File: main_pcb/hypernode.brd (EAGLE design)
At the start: 92.5 x 100 mm, 134 parts, among them IC1 74HCT245D, J1 AVR_SPI_PRG_62X3_LOCK, U1 MAX488, U2 PCA9685, U3 VOLTAGE_REGULATORDPACK, U4 ATMEGA328P, U5 MAX3421E, X1 USB-A-H, X10 JST-XH-03-PIN-LONG-PAD, X2 JST-XH-CONNECTOR-02-PIN, X4 JST-XH-CONNECTOR-02-PIN, X7 JST-XH-03-PIN-LONG-PAD, X8 JST-XH-03-PIN-LONG-PAD, X9 JST-XH-03-PIN-LONG-PAD, Y1 8MHZ

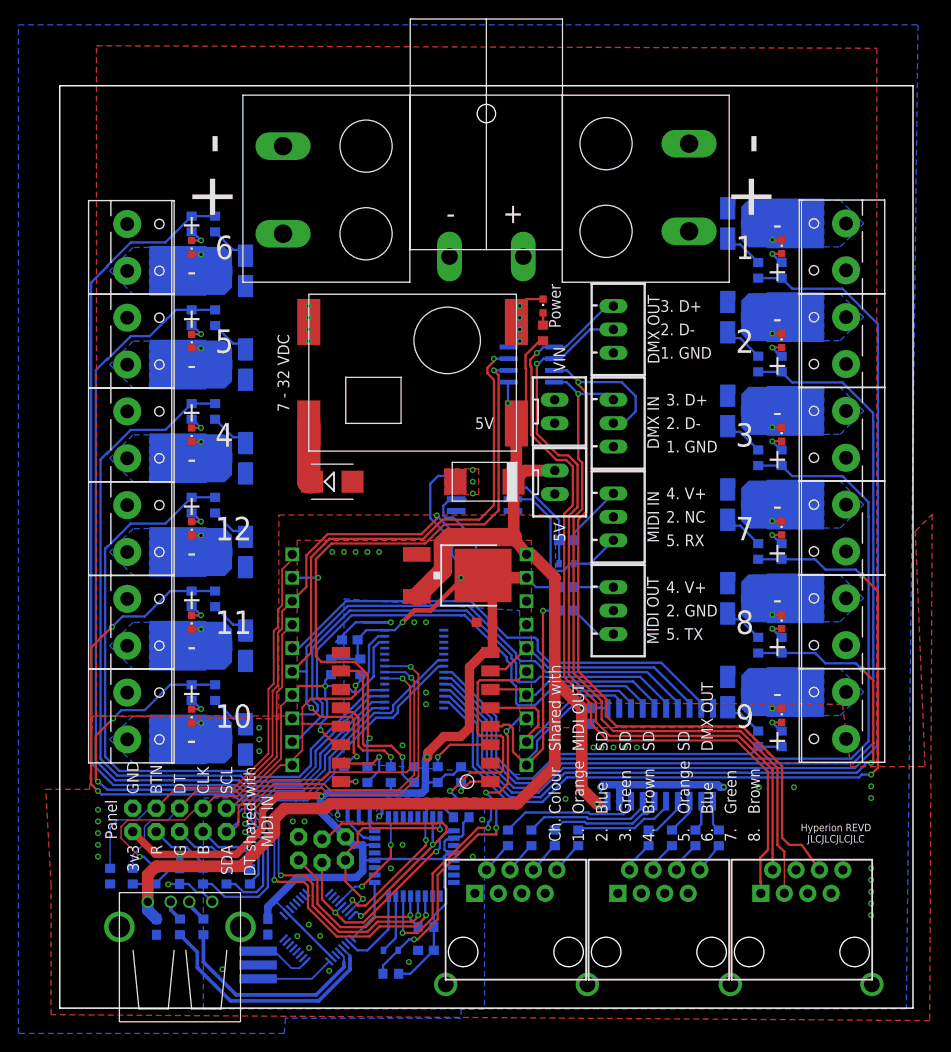
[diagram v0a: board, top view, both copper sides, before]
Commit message: remove unnecessary components from main pcb
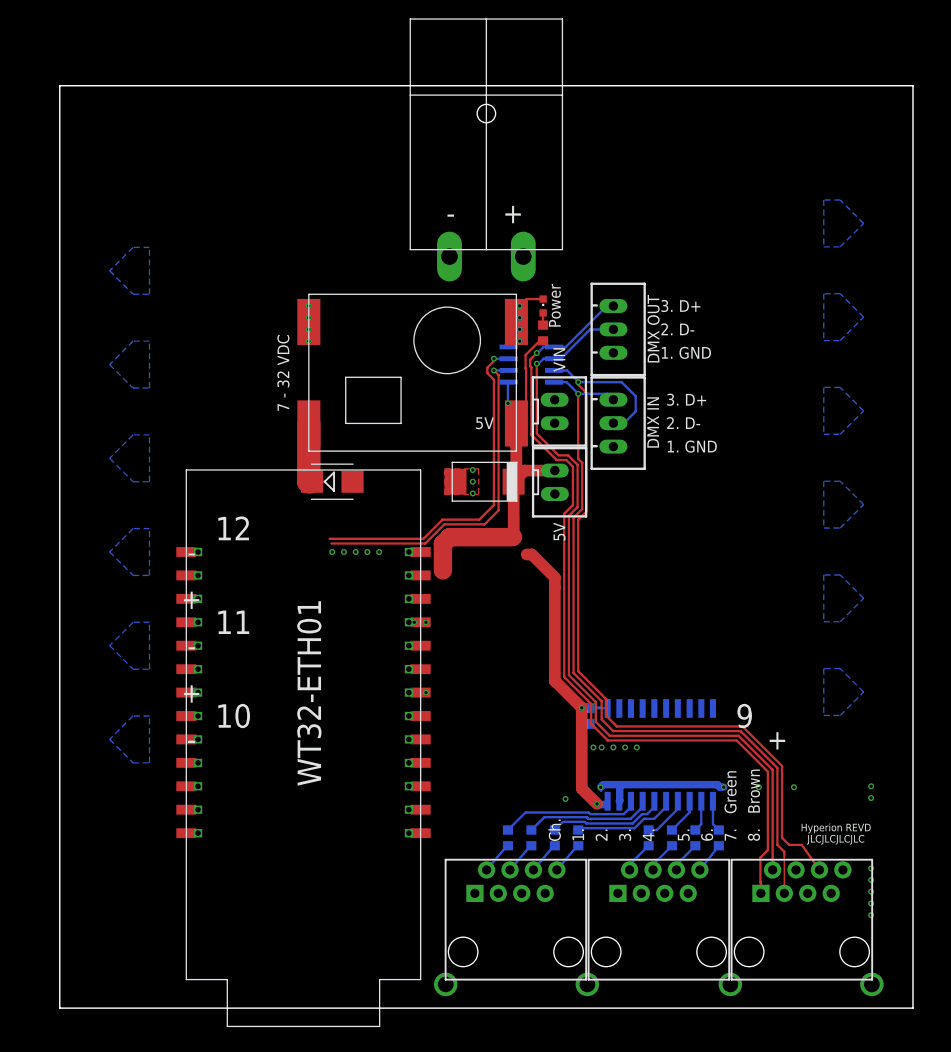
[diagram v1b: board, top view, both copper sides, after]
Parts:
- removed C2, C3, C4, C6, C7: 100nF, Multischriever:ADAFRUIT_C0603
- removed C8: 1uF, Multischriever:ADAFRUIT_C0603
- removed C9: 4.7uF, Multischriever:ADAFRUIT_C0603
- removed D1, D3: (no value), Multischriever:ADAFRUIT_SOD-523
- removed HCPL0453: HCPL0700, optocoupler:SOIC08
- removed J1: AVR_SPI_PRG_62X3_LOCK, SparkFun-Connectors:2X3_LOCK
- removed LED11, LED13, LED14, LED15, LED16, LED17, LED18, LED2, LED3, LED5, LED7, LED9: (no value), Multischriever:ADAFRUIT_CHIPLED_0603
- removed R12, R15, R18, R19, R22, R23, R26, R27, R3, R30, R31, R32, R33, R34, R35, R36, R37, R38, R39, R40, R41, R5: (no value), Multischriever:ADAFRUIT_R0603
- removed R13, R45, R46, R47: 180R, Multischriever:ADAFRUIT_R0603
- removed R14: 1K, Multischriever:ADAFRUIT_R0603
- removed R21, R24: 1k, Multischriever:ADAFRUIT_R0603
- removed R25, R28, R29, R42: 10k, Multischriever:ADAFRUIT_R0603
- removed R43, R44, R57: 4k7, Multischriever:ADAFRUIT_R0603
- removed R48, R50, R55, R56: 10K, Multischriever:ADAFRUIT_R0603
- removed R49, R9: 470R, Multischriever:ADAFRUIT_R0603
- removed R52: 100R, Multischriever:ADAFRUIT_R0603
- removed R53, R54, R6, R7: 33R, Multischriever:ADAFRUIT_R0603
- removed R8: 220R, Multischriever:ADAFRUIT_R0603
- removed REMOTE: M05X2NO_SILK, SparkFun-Connectors:2X5_NOSILK
- removed U$1: ESP32POE, Multischriever:ESP32POE
- removed U$10, U$12, U$14, U$16, U$18, U$19, U$20, U$21, U$22, U$23, U$5, U$7: NCV8401_LOAD_SWITCH'DPAK+SOT23', Multischriever:DPACK+SOT23
- removed U$2, U$6: BIGTERMINAL, Multischriever:BIGTERMINAL2P
- removed U$24: 12MHz, adafruit:AWCSR
- removed U$9: ESP8266_ESP12NOSILK, Multischriever:ESP8266-ESP12_ESP8266-ESP12_NOSILK
- removed U2: PCA9685, SparkFun-DigitalIC:TSSOP-28_4MM
- removed U3: VOLTAGE_REGULATORDPACK, Multischriever:SPARKFUN-POWERIC_V-REG_DPACK
- removed U4: ATMEGA328P, SparkFun-DigitalIC:TQFP32-08
- removed U5: MAX3421E, SparkFun-DigitalIC:TQFP32-5MM
- removed X1: USB-A-H, con-usb:USB-A-H
- removed X10, X9: JST-XH-03-PIN-LONG-PAD, Rembrandt Electronics - JST XH Connectors v1-0:JST-XH-03-PACKAGE-LONG-PAD
- removed X11, X14, X16, X17, X19, X21, X22, X23, X24, X25, X26, X3: (no value), Multischriever:CON-WAGO-508_W237-132PLUGGABLE
- removed Y1: 8MHZ, SparkFun-FreqCtrl:RESONATOR-SMD
- added U$17: WT32-ETH01, Multischriever:WT32-ETH01
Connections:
- removed net ENCA: R48.2, REMOTE.8, U$1.GPI34_BUT1
- removed net ENCBTN: R49.2, REMOTE.4, U$1.GPI39
- removed net MIDIIN: R50.2, R52.2, REMOTE.6, U$1.GPI35
- removed net N$1: R45.1, REMOTE.3
- removed net N$11: R45.2, U2.20
- removed net N$12: R46.1, REMOTE.5
- removed net N$14: R6.1, X10.1
- removed net N$15: R7.1, X10.3
- removed net N$17: D1.A, HCPL0453.3, X9.3
- removed net N$19: R5.1, U$7.B, U$7.B_
- removed net N$20: R8.1, X9.1
- removed net N$21: D1.K, HCPL0453.2, R8.2
- removed net N$22: LED2.A, R3.1
- removed net N$23: R29.1, U$9.9
- removed net N$24: LED2.C, U$7.C, U$7.C_, X3.2
- removed net N$27: R42.1, U$9.11
- removed net N$29: R21.2, U$9.8
- removed net N$30: R24.2, U$9.7
- removed net N$31: R28.2, U$9.4
- removed net N$32: R25.2, U$9.2
- removed net N$33: R47.1, REMOTE.7
- removed net N$35: R15.1, U$10.B, U$10.B_
- removed net N$36: LED5.A, R12.1
- removed net N$37: LED5.C, U$10.C, U$10.C_, X11.2
- removed net N$39: HCPL0453.6, R52.1, R9.2
- removed net N$40: U4.7, Y1.1
- removed net N$41: U4.8, Y1.3
- removed net N$42: U4.9, U5.12
- removed net N$43: R54.1, X1.D+
- removed net N$44: R53.1, X1.D-
- removed net N$45: LED3.C, U$5.C, U$5.C_, X17.2
- removed net N$46: R14.1, U$5.B, U$5.B_
- removed net N$47: R19.1, U$12.B, U$12.B_
- removed net N$48: LED7.A, R18.1
- removed net N$49: LED7.C, U$12.C, U$12.C_, X14.2
- removed net N$50: R53.2, U5.20
- removed net N$51: R54.2, U5.21
- removed net N$52: U$24.3, U5.24
- removed net N$53: U$24.1, U5.25
- removed net N$54: U4.32, U5.18
- removed net N$55: U4.1, U5.17
- removed net N$56: J1.4, U4.15, U5.16
- removed net N$57: J1.1, U4.16, U5.15
- removed net N$58: J1.3, U4.17, U5.13
- removed net N$59: R23.1, U$14.B, U$14.B_
- removed net N$60: LED9.A, R22.1
- removed net N$61: LED9.C, U$14.C, U$14.C_, X16.2
- removed net N$62: LED3.A, R13.1
- removed net N$63: R56.1, U4.14, U5.14
- removed net N$64: J1.5, R55.1, U4.29
- removed net N$68: D3.K, U4.31
- removed net N$7: R47.2, U2.22
- removed net N$71: R27.1, U$16.B, U$16.B_
- removed net N$72: LED11.A, R26.1
- removed net N$73: LED11.C, U$16.C, U$16.C_, X19.2
- removed net N$77: R31.1, U$18.B, U$18.B_
- removed net N$78: LED13.A, R30.1
- removed net N$79: LED13.C, U$18.C, U$18.C_, X21.2
- removed net N$80: R33.1, U$19.B, U$19.B_
- removed net N$81: LED14.A, R32.1
- removed net N$82: LED14.C, U$19.C, U$19.C_, X22.2
- removed net N$83: R35.1, U$20.B, U$20.B_
- removed net N$84: LED15.A, R34.1
- removed net N$85: LED15.C, U$20.C, U$20.C_, X23.2
- removed net N$86: R37.1, U$21.B, U$21.B_
- removed net N$87: LED16.A, R36.1
- removed net N$88: LED16.C, U$21.C, U$21.C_, X24.2
- removed net N$89: R39.1, U$22.B, U$22.B_
- removed net N$9: R46.2, U2.21
- removed net N$90: LED17.A, R38.1
- removed net N$91: LED17.C, U$22.C, U$22.C_, X25.2
- removed net N$92: R41.1, U$23.B, U$23.B_
- removed net N$93: LED18.A, R40.1
- removed net N$94: LED18.C, U$23.C, U$23.C_, X26.2
- removed net SCL: R44.1, REMOTE.10, U$1.GPIO16_I2C_SCL, U$9.6, U2.26, U4.28
- removed net SDA: R43.1, REMOTE.9, U$1.GPIO13_I2C_SDA, U$9.5, U2.27, U4.27
- removed net T1DRIVE1: R13.2, R14.2, U2.15
- removed net T1DRIVE10: R34.2, R35.2, U2.13
- removed net T1DRIVE11: R32.2, R33.2, U2.12
- removed net T1DRIVE12: R30.2, R31.2, U2.8
- removed net T1DRIVE2: R3.2, R5.2, U2.16
- removed net T1DRIVE3: R12.2, R15.2, U2.17
- removed net T1DRIVE4: R18.2, R19.2, U2.18
- removed net T1DRIVE5: R22.2, R23.2, U2.7
- removed net T1DRIVE6: R26.2, R27.2, U2.6
- removed net T1DRIVE7: R40.2, R41.2, U2.11
- removed net T1DRIVE8: R38.2, R39.2, U2.10
- removed net T1DRIVE9: R36.2, R37.2, U2.9
- removed net USBRX: D3.A, R57.2, U$1.GPIO3_U0RXD
- removed net USBTX: U$1.GPIO1_U0TXD, U4.30
- new net DMXOUT: U$17.P$8, U$17.P_TXD, U1.3
- net +3V3: now also U$17.3V3, U$17.3V3@1, U$17.P_3V3, U$17.P_3V3@1; no longer C2.1, C3.1, C4.1, C6.1, C7.1, C8.1, HCPL0453.8, J1.2, R28.1, R29.2, R42.2, R43.2, R44.2, R48.1, R50.1, R55.2, R56.2, R57.1, R6.2, R9.1, REMOTE.1, U$1.+3V3, U$9.16, U2.28, U3.4, U4.18, U4.20, U4.4, U4.6, U5.2, U5.23
- net +5V: now also U$17.5V, U$17.P_5V; no longer C9.1, U$1.+5V, U3.3, X1.VBUS
- net DMXIN: now also U$17.IO36, U$17.P_IO36; no longer R24.1, U$1.GPI36_U1RXD
- net GND: now also U$17.GND, U$17.GND@1, U$17.GND@2, U$17.GND@3, U$17.GND@4, U$17.P_GND, U$17.P_GND@1, U$17.P_GND@2, U$17.P_GND@3, U$17.P_GND@4; no longer C2.2, C3.2, C4.2, C6.2, C7.2, C8.2, C9.2, HCPL0453.5, J1.6, R25.1, R49.1, REMOTE.2, U$1.GND, U$10.E, U$10.E_, U$12.E, U$12.E_, U$14.E, U$14.E_, U$16.E, U$16.E_, U$18.E, U$18.E_, U$19.E, U$19.E_, U$2.P$1, U$20.E, U$20.E_, U$21.E, U$21.E_, U$22.E, U$22.E_, U$23.E, U$23.E_, U$24.2, U$5.E, U$5.E_, U$6.P$2, U$7.E, U$7.E_, U$9.1, U2.1, U2.14, U2.2, U2.23, U2.24, U2.25, U2.3, U2.4, U2.5, U3.1, U4.21, U4.3, U4.5, U5.19, U5.3, X1.GND, X10.2, Y1.2
- net VDD: no longer U$2.P$2, U$6.P$1, X11.1, X14.1, X16.1, X17.1, X19.1, X21.1, X22.1, X23.1, X24.1, X25.1, X26.1, X3.1
- net WS1: now also U$17.P_RXD, U$17.RXD; no longer R7.2, U$1.GPIO5_SPL_CS, U$9.12
- net WS2: now also U$17.IO4, U$17.P_IO4; no longer U$1.GPIO4_U1TXD, U$9.13
- net WS3: now also U$17.IO14, U$17.P_IO14; no longer U$1.GPIO14_HS2_CLK
- net WS4: now also U$17.IO2, U$17.P_IO2; no longer U$1.GPIO2_HS2_DATA0, U$9.14
- net WS5: now also U$17.IO15, U$17.P_IO15; no longer U$1.GPIO15_HS2_CMD
- net WS6: now also U$17.CFG, U$17.P_CFG; no longer R21.1, U$1.GPIO32, U1.3
- net WS7: now also U$17.IO0, U$17.P_IO0; no longer U$1.GPIO0, U$9.15
- net WS8: now also U$17.485_EN, U$17.P_485_EN; no longer U$1.GPIO33
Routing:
- net +3V3: track 207.2 -> 0.00 mm, vias 5 -> 0
- net WS6: track 120.3 -> 0.00 mm, vias 3 -> 0
- net T1DRIVE7: track 117.1 -> 0.00 mm
- net T1DRIVE1: track 106.3 -> 0.00 mm
- net T1DRIVE8: track 105.9 -> 0.00 mm
- net T1DRIVE2: track 95.3 -> 0.00 mm
- net T1DRIVE9: track 94.7 -> 0.00 mm
- net T1DRIVE10: track 89.2 -> 0.00 mm, vias 2 -> 0
- net T1DRIVE3: track 84.2 -> 0.00 mm
- net T1DRIVE11: track 77.7 -> 0.00 mm, vias 2 -> 0
- net T1DRIVE5: track 77.5 -> 0.00 mm, vias 2 -> 0
- net SCL: track 74.4 -> 0.00 mm, vias 4 -> 0
- net SDA: track 74.4 -> 0.00 mm, vias 3 -> 0
- net T1DRIVE4: track 73.0 -> 0.00 mm
- net +5V: track 154.0 -> 83.2 mm
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- removed copper zone on layer 16, net GND
- removed copper zone on layer 1, net VDD
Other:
- board text removed: "+ -"
- board text removed: "1"
- board text removed: "2"
- board text removed: "2. GND"
- board text removed: "2. NC"
- board text removed: "3"
- board text removed: "3v3"
- board text removed: "4"
- board text removed: "4. V+"
- board text removed: "5"
- board text removed: "5. RX"
- board text removed: "5. TX"
- board text removed: "6"
- board text removed: "7"
- board text removed: "8"
- board text removed: "B"
- board text removed: "BTN"
- board text removed: "Blue"
- board text removed: "CLK"
- board text removed: "Colour"
- board text removed: "DT"
- board text removed: "DT shared with MIDI IN"
- board text removed: "G"
- board text removed: "GND"
- board text removed: "MIDI IN"
- board text removed: "MIDI OUT"
- board text removed: "NCV8401B IRLR8729 IRLML6344"
- board text removed: "Orange"
- board text removed: "Panel"
- board text removed: "R"
- board text removed: "SCL"
- board text removed: "SD"
- board text removed: "SDA"
- board text removed: "Shared with"

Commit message: further cleanup and arrangement
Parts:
- removed R10: 100R, Multischriever:ADAFRUIT_R0603
- added C2: 100nF, Multischriever:ADAFRUIT_C0603
- added LED2: (no value), Multischriever:ADAFRUIT_CHIPLED_0603
- added PROGRAM: (no value), pinhead:1X06
- added R3: 100R, Multischriever:ADAFRUIT_R0603
- added R5: 180R, Multischriever:ADAFRUIT_R0603
- moved LED1 87.0 mm to (6.29, 0.00), turned to 90 degrees
- moved R51 83.0 mm to (6.29, 1.91), turned to 180 degrees
- moved U1 49.5 mm to (78.7, 26.0), flipped to the top, turned to 270 degrees
- moved D2 28.7 mm to (55.8, 66.7)
- moved X7 28.0 mm to (75.5, 47.6)
- moved X8 28.0 mm to (75.5, 37.5)
- moved C5 10.9 mm to (68.5, 30.5), flipped to the top
- moved IC1 5.81 mm to (59.6, 26.0), flipped to the top
- moved C1 4.96 mm to (49.5, 50.8), turned to 270 degrees
- moved X2 2.69 mm to (55.8, 60.3)
- moved X4 2.69 mm to (55.8, 52.6)
- moved U$17 2.62 mm to (17.1, 47.6)
- moved R1 2.54 mm to (46.3, 16.0), flipped to the top
- moved R11 2.54 mm to (53.9, 16.0), flipped to the top
- moved R2 2.54 mm to (48.8, 16.0), flipped to the top
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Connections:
- removed net N$10: IC1.13, R16.1
- removed net N$18: R20.2, U$11.6
- removed net N$25: R16.2, U$11.4
- removed net N$26: R10.2, U$11.2
- removed net N$28: R4.2, U$13.6
- removed net N$3: IC1.18, R1.1
- removed net N$5: IC1.17, R2.1
- removed net N$6: IC1.16, R4.1
- removed net N$8: IC1.14, R10.1
- removed net NIKS: IC1.15, R11.1
- removed net WS1-2: R1.2, U$13.2
- removed net WS2-2: R2.2, U$13.4
- removed net WS4-2: R11.2, U$13.8
- new net N$1: LED2.A, R5.1
- new net N$11: IC1.17, R20.1
- new net N$12: IC1.16, R16.1
- new net N$14: IC1.14, R11.1
- new net N$15: IC1.13, R4.1
- new net N$17: IC1.11, R1.1
- new net N$9: IC1.18, R17.1
- net +5V: now also C2.1
- net GND: now also C2.2, LED2.C
- net N$13: now also IC1.15, R3.1; no longer IC1.12, R20.1
- net N$16: now also IC1.12, R2.1; no longer IC1.11, R17.1
- net N$2: now also R5.2, U$17.IO12, U$17.P_IO12; no longer R17.2, U$11.8
- net WS1: now also IC1.5; no longer IC1.2
- net WS2: now also IC1.4; no longer IC1.3
- net WS3: now also IC1.3; no longer IC1.4
- net WS4: now also IC1.2; no longer IC1.5
- net WS5: now also IC1.9; no longer IC1.6
- net WS6: now also IC1.8; no longer IC1.7
- net WS7: now also IC1.7; no longer IC1.8
- net WS8: now also IC1.6; no longer IC1.9
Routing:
- net DMXZ: track 85.0 -> 0.00 mm, vias 1 -> 0
- net DMXY: track 89.9 -> 5.06 mm, vias 1 -> 0
- net DMXB: track 87.7 -> 5.78 mm, vias 1 -> 0
- net DMXA: track 79.5 -> 5.57 mm, vias 1 -> 0
- net +5V: track 83.2 -> 18.4 mm, vias 3 -> 1
- net DMXOUT: track 37.4 -> 0.00 mm, vias 1 -> 0
- net DMXIN: track 36.6 -> 0.00 mm, vias 1 -> 0
- net N$4: track 6.66 -> 28.8 mm
- net GND: track 22.4 -> 2.84 mm, vias 40 -> 15
- net N$3: track 15.1 -> 0.00 mm
- net N$5: track 13.9 -> 0.00 mm
- net N$6: track 12.6 -> 0.00 mm
- net NIKS: track 11.3 -> 0.00 mm
- net N$8: track 5.03 -> 0.00 mm
- net N$10: track 3.91 -> 0.00 mm
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- removed copper zone on layer 16, net N$24
- removed copper zone on layer 16, net N$37
- removed copper zone on layer 16, net N$45
- removed copper zone on layer 16, net N$49
- removed copper zone on layer 16, net N$61
- removed copper zone on layer 16, net N$73
- removed copper zone on layer 16, net N$79
- removed copper zone on layer 16, net N$82
- removed copper zone on layer 16, net N$85
- removed copper zone on layer 16, net N$88
- removed copper zone on layer 16, net N$91
- removed copper zone on layer 16, net N$94
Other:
- outline, holes or cut-outs redrawn
- board text added: "Connection"
- board text removed: "+"
- board text removed: "-"
- board text removed: "1."
- board text removed: "10"
- board text removed: "11"
- board text removed: "12"
- board text removed: "2."
- board text removed: "3."
- board text removed: "4."
- board text removed: "5."
- board text removed: "6."
- board text removed: "7."
- board text removed: "8."
- board text removed: "9"
- board text removed: "Brown"
- board text removed: "Ch."
- board text removed: "Green"

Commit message: programmer
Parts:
- added R7: 10K, Multischriever:ADAFRUIT_R0603
- U$17: value WT32-ETH01 -> WT32-ETH01WT32-ETH01-SMD; device Multischriever:WT32-ETH01 -> Multischriever:WT32-ETH01-SMD
- moved U$4 0.64 mm to (83.8, 20.3)
- renumbered LED1 to LED_PWR, LED2 to LED_STATUS
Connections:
- removed net N$2: R5.2, U$17.IO12, U$17.P_IO12
- new net EN: PROGRAM.4, U$17.P_EN, U$17.P_EN@1
- new net N$10: R2.2, U$13.4
- new net N$18: R4.2, U$13.6
- new net N$19: R11.2, U$13.8
- new net N$3: R3.2, U$11.2
- new net N$5: R16.2, U$11.4
- new net N$6: R20.2, U$11.6
- new net N$7: R17.2, U$11.8
- new net N$8: R1.2, U$13.2
- new net RX: PROGRAM.3, U$17.P_RX0
- new net TX: PROGRAM.2, U$17.P_TX0
- net +3V3: now also PROGRAM.1; no longer U$17.3V3, U$17.3V3@1
- net +5V: no longer U$17.5V
- net DMXIN: no longer U$17.IO36
- net DMXOUT: now also R5.1; no longer U$17.P$8
- net GND: now also PROGRAM.6, R7.2; no longer U$17.GND, U$17.GND@1, U$17.GND@2, U$17.GND@3, U$17.GND@4
- net N$1: now also R5.2; no longer R5.1
- net WS1: no longer U$17.RXD
- net WS2: no longer U$17.IO4
- net WS3: no longer U$17.IO14
- net WS4: now also R7.1; no longer U$17.IO2
- net WS5: no longer U$17.IO15
- net WS6: no longer U$17.CFG
- net WS7: now also PROGRAM.5, U$17.P_IO12; no longer U$17.IO0, U$17.P_IO0
- net WS8: no longer U$17.485_EN
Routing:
- net +5V: track 18.4 -> 14.8 mm, vias 1 -> 0
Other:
- board text added: "DISCONNECT BOOT TO USE ETH"
- board text added: "GND BOOT EN RX TX 3V3"
- board text added: "HyperNode REVA JLCJLCJLCJLC"
- board text added: "SHARED WITH DMX"
- board text added: "Status"
- board text removed: "Connection"
- board text removed: "Hyperion REVD JLCJLCJLCJLC"

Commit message: routing
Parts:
- removed U$8: POWERPOLE, Multischriever:POWERPOLEPCBMOUNT
- added R6: 180R, Multischriever:ADAFRUIT_R0603
- R5: value 180R -> 1K
- moved R5 53.7 mm to (45.7, 45.7), turned to 270 degrees
- moved PROGRAM 20.1 mm to (10.8, 47.0)
- moved R7 1.42 mm to (44.5, 19.1), turned to 270 degrees
- moved C5 0.90 mm to (67.9, 29.8)
- moved U1 0.90 mm to (78.0, 25.4)
- moved C2 0.90 mm to (81.9, 26.7)
- moved IC1 0.64 mm to (59.6, 25.4)
- moved LED_PWR 0.56 mm to (6.86, 0.00)
- moved R51 0.56 mm to (6.86, 1.91)
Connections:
- new net N$2: LED_STATUS.A, R6.1
- new net N$20: U$17.P_3V3@1
- net +3V3: no longer U$17.P_3V3@1
- net DMXOUT: no longer R5.1
- net EN: no longer U$17.P_EN@1
- net GND: no longer U$8.P$2
- net N$1: now also PROGRAM.3, R5.1; no longer LED_STATUS.A, R5.2
- net RX: now also R5.2, R6.2; no longer PROGRAM.3
- net VDD: no longer U$8.P$1
- net WS1: now also U$17.P_IO14; no longer U$17.P_RXD
- net WS2: now also U$17.P_IO12; no longer U$17.P_IO4
- net WS3: now also U$17.P_IO4; no longer U$17.P_IO14
- net WS4: now also PROGRAM.5
- net WS6: now also U$17.P_RXD; no longer U$17.P_CFG
- net WS7: now also U$17.P_485_EN; no longer PROGRAM.5, U$17.P_IO12
- net WS8: now also U$17.P_CFG; no longer U$17.P_485_EN
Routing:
- net +5V: track 14.8 -> 151.2 mm
- net WS4: track 0.00 -> 99.8 mm, vias 0 -> 1
- net RX: track 0.00 -> 69.7 mm
- net DMXOUT: track 0.00 -> 67.2 mm, vias 0 -> 4
- net DMXY: track 5.06 -> 63.3 mm, vias 0 -> 2
- net DMXZ: track 0.00 -> 56.6 mm, vias 0 -> 2
- net DMXA: track 5.57 -> 59.0 mm
- net WS8: track 0.00 -> 47.1 mm, vias 0 -> 2
- net WS7: track 0.00 -> 44.1 mm, vias 0 -> 2
- net DMXIN: track 0.00 -> 42.7 mm, vias 0 -> 2
- net WS6: track 0.00 -> 42.1 mm, vias 0 -> 2
- net DMXB: track 5.78 -> 42.9 mm
- net N$1: track 0.00 -> 35.3 mm, vias 0 -> 1
- net TX: track 0.00 -> 33.9 mm, vias 0 -> 1
- net GND: track 2.84 -> 34.3 mm, vias 15 -> 28
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- added copper zone on layer 1, net +5V
- added copper zone on layer 16, net GND
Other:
- board text added: "SHARED WITH RX"
- board text removed: "- +"
- board text removed: "SHARED WITH DMX"
